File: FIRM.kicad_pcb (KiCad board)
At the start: 8 copper layers, 21.3 x 27 mm, 99 parts, among them J1 DM3CS-SF, J2 Conn_01x02_Pin, Q1 IRLML6402, U1 W25Q128JVS, U2 STM32F405RGTx, U3 ADXL371, U5 INA219AxDCN, U6 MIC5219-3.3YM5, U9 A-USBC-20F0-EA-GSR05, X1 32.768khz, Y1 12 MHz

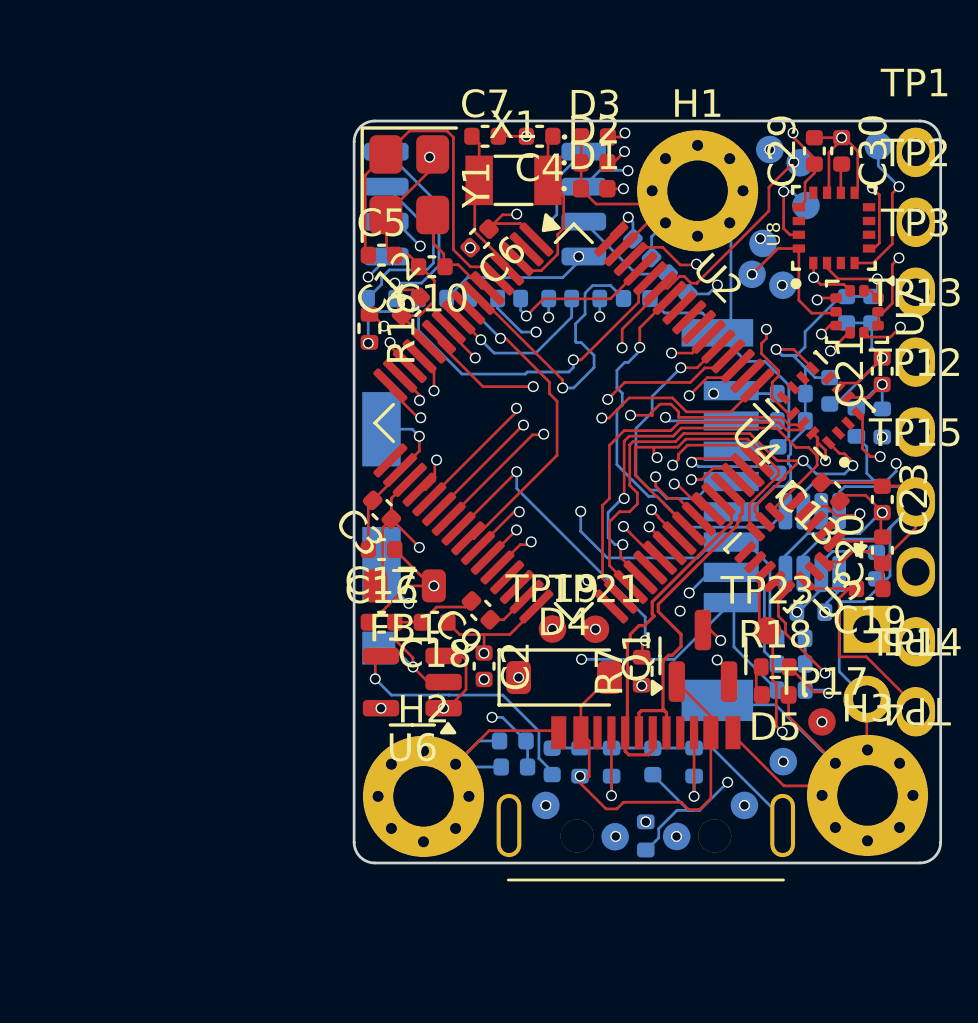
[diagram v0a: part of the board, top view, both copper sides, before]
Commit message: resistor arrays and smaller parts
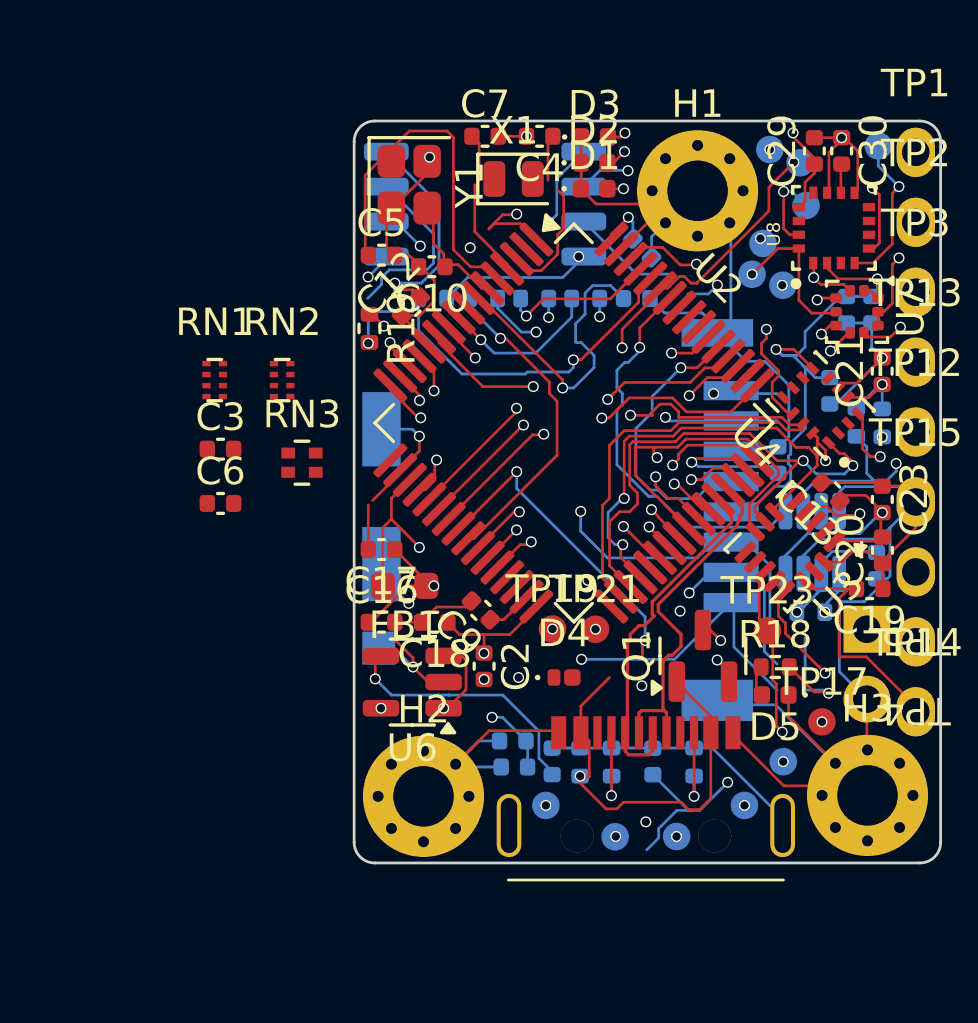
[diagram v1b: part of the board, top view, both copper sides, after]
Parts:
- removed R1, R5, R6, R7: 10k, Resistor_SMD:R_0402_1005Metric
- removed R10, R2, R4, R8, R9: 47k, Resistor_SMD:R_0402_1005Metric
- added RN1: 47k, connectors:R_Array_YC104, F.Cu at (148.3, 84.0)
- added RN2: 10k, connectors:R_Array_YC104, F.Cu at (150.7, 84.0)
- added RN3: 47k, connectors:R_Array_EXB-24V, F.Cu at (151.4, 87.0)
- D4: footprint Diode_SMD:D_SOD-123 -> connectors:D_schottky_NSR05F30NXT5G
- FB1: footprint Inductor_SMD:L_0805_2012Metric -> Inductor_SMD:L_0603_1608Metric
- X1: footprint Crystal:Crystal_SMD_3215-2Pin_3.2x1.5mm -> connectors:Crystal_ECS-.327-6-12RR-TR
- Y1: footprint Crystal:Crystal_SMD_Abracon_ABM8G-4Pin_3.2x2.5mm -> connectors:Crystal_ECS-120-10-36B2-CWY-TR
- moved C6 13.5 mm to (148.5, 88.5), turned to 0 degrees
- moved C3 6.27 mm to (148.5, 86.5), turned to 0 degrees

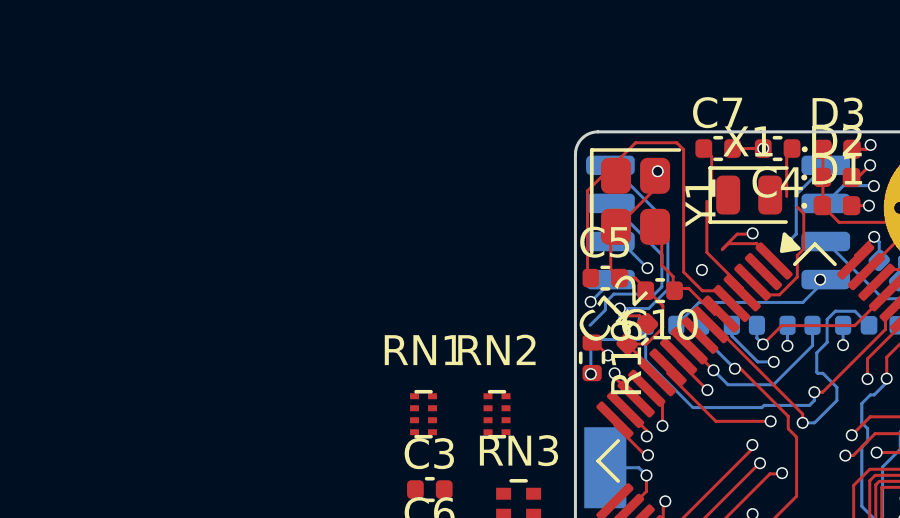
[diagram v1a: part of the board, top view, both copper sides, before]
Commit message: new flash chip
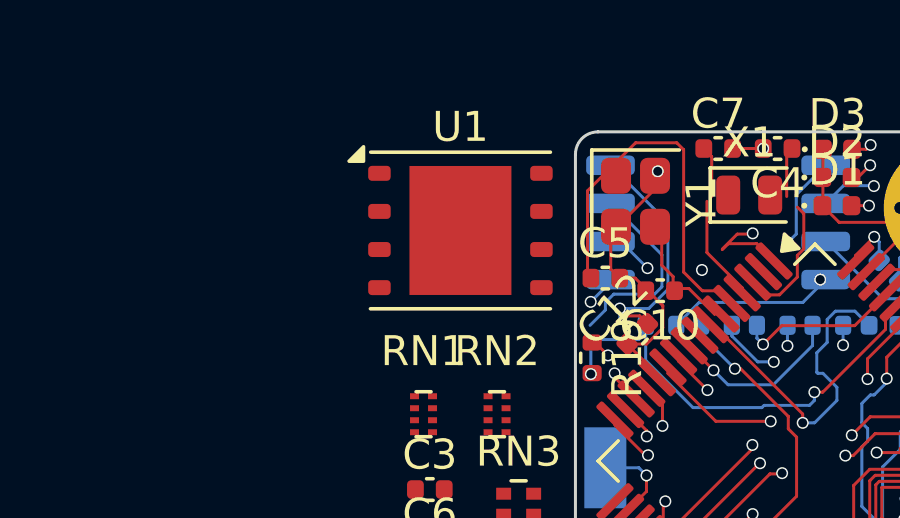
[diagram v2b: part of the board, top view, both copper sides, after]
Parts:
- added U1: W25Q128JVP, Package_SON:WSON-8-1EP_6x5mm_P1.27mm_EP3.4x4.3mm, F.Cu at (149.5, 77.9)

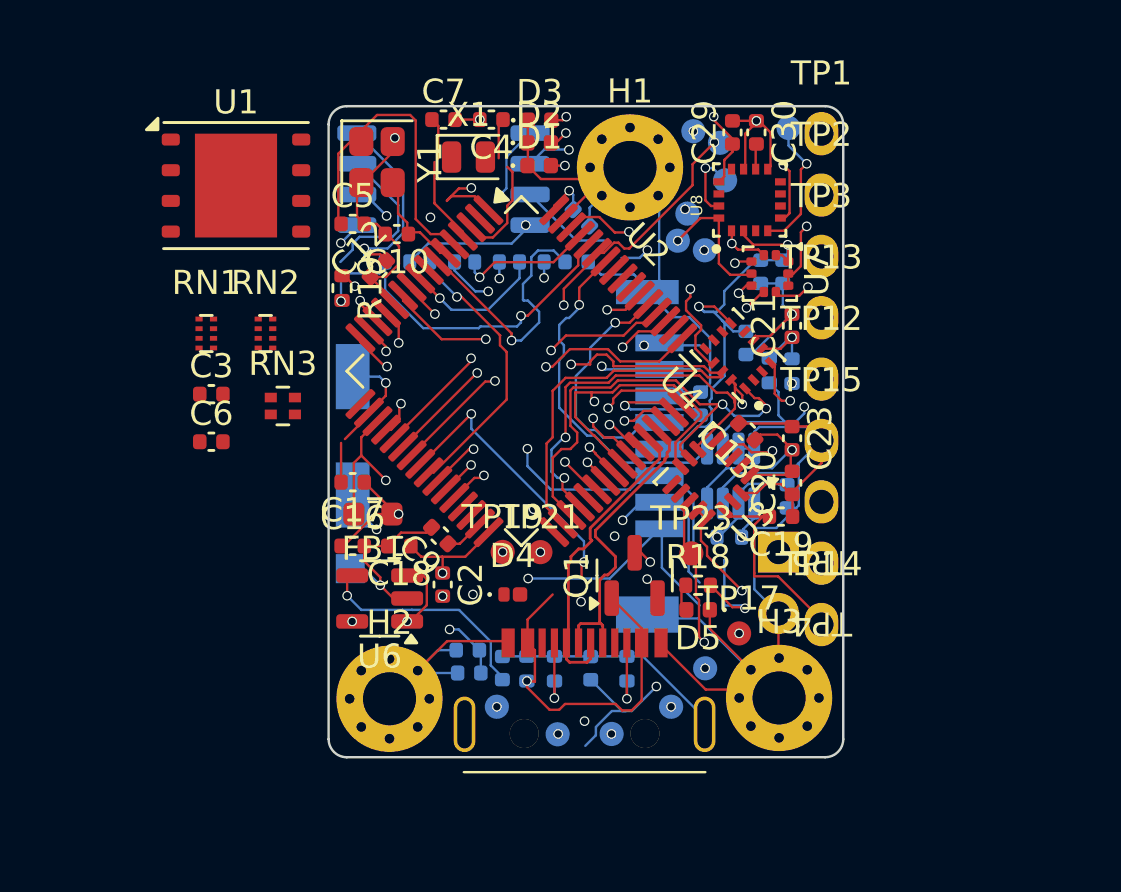
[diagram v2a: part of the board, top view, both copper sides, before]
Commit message: cleanup and improved decoupling capacitor locations
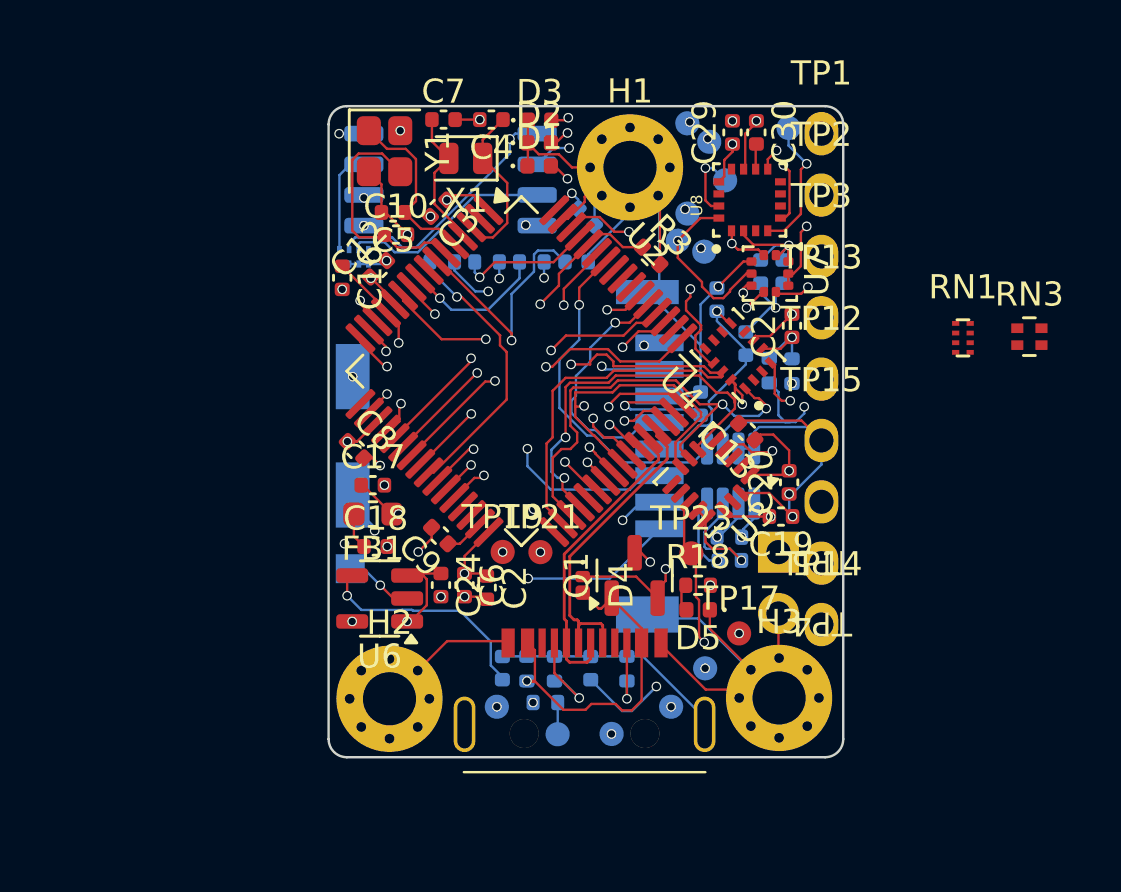
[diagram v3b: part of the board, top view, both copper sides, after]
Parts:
- removed the U1 at (149.5, 77.9)
- removed the U1 at (158.1, 77.6)
- added U1: W25Q128JVP, Package_SO:SOIC-8_5.3x5.3mm_P1.27mm, B.Cu at (158.4, 77.6)
- C23, R19, RN2: moved to B.Cu
- C24, C8, R3: moved to F.Cu
- moved RN1 31.3 mm to (179.6, 84.2)
- moved RN3 31.0 mm to (182.3, 84.1)
- moved R19 19.1 mm to (162.3, 99.3), turned to 180 degrees
- moved C11 17.8 mm to (170.6, 84.4), turned to -90 degrees
- moved C24 14.8 mm to (158.0, 94.4)
- moved C3 12.2 mm to (157.9, 78.8), turned to -135 degrees
- moved C6 12.0 mm to (159.0, 94.4), turned to -90 degrees
- moved C16 11.1 mm to (153.9, 81.7), turned to -90 degrees
- moved R3 10.5 mm to (166.7, 80.8), turned to -45 degrees
- moved C8 9.51 mm to (154.4, 88.8), turned to -45 degrees
- moved C23 5.68 mm to (169.9, 93.4), turned to 180 degrees
- moved RN2 4.85 mm to (154.4, 80.8), turned to -90 degrees
- moved D4 2.92 mm to (163.9, 94.4), turned to -90 degrees
- moved C22 2.16 mm to (169.4, 82.6), turned to 90 degrees
- moved C2 1.83 mm to (159.9, 94.5)
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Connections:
- RN1 pad 1: /SDIO_D0 -> /SDIO_D2
- RN1 pad 2: /SDIO_CMD -> /SDIO_D3
- RN1 pad 3: /SDIO_D3 -> /SDIO_CMD
- RN1 pad 4: /SDIO_D2 -> /SDIO_D0
- RN2 pad 2: Net-(RN2-R2.1) -> /FLASH_CS
- RN2 pad 3: /FLASH_CS -> Net-(RN2-R3.1)
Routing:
- net +3.3V: track 91.5 -> 55.8 mm
- net GND: track 142.1 -> 109.7 mm, vias 12 -> 26
- net Net-(R19-Pad1): track 23.6 -> 1.31 mm, vias 2 -> 0
- net /SD_DETECT: track 22.5 -> 9.67 mm, vias 3 -> 2
- net /BOOT0: track 14.5 -> 25.1 mm
- net Net-(RN2-R3.1): track 0.00 -> 8.81 mm
- net /I2C1_SDA: track 29.1 -> 35.4 mm
- net /HSE_OUT: track 3.54 -> 9.08 mm
- net /VSENS_IN: track 14.3 -> 9.05 mm, vias 3 -> 2
- net /SDIO_CMD: track 21.6 -> 16.4 mm
- net /HSE_IN: track 12.3 -> 7.44 mm
- net /SDIO_D3: track 19.6 -> 15.2 mm
- net /SDIO_D2: track 23.7 -> 19.8 mm
- net Net-(RN2-R2.1): track 3.85 -> 0.00 mm
- net Net-(RN2-R1.1): track 6.56 -> 3.71 mm
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
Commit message: added back resistors
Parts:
- removed RN1: 47k, connectors:R_Array_YC104
- removed RN3: 47k, connectors:R_Array_EXB-24V
- added R1: 47k, Resistor_SMD:R_0402_1005Metric, F.Cu at (177.2, 84.0)
- added R2: 47k, Resistor_SMD:R_0402_1005Metric, F.Cu at (177.2, 85.4)
- added R4: 47k, Resistor_SMD:R_0402_1005Metric, F.Cu at (177.2, 87.4)
- added R5: 47k, Resistor_SMD:R_0402_1005Metric, F.Cu at (177.2, 89.4)
- added R6: 47k, Resistor_SMD:R_0402_1005Metric, F.Cu at (162.0, 94.9)
- added R7: 47k, Resistor_SMD:R_0402_1005Metric, B.Cu at (159.0, 97.2)
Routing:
- net /SDIO_D1: track 7.58 -> 19.8 mm, vias 2 -> 3
- net /SD_DETECT: track 9.67 -> 21.6 mm, vias 2 -> 1
- net /SDIO_D0: track 8.51 -> 6.93 mm, vias 2 -> 1

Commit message: finished routing resistors
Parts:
- R1, R2, R4, R5: moved to B.Cu
- moved R1 14.5 mm to (169.2, 96.2)
- moved R2 12.7 mm to (169.2, 95.2)
- moved R4 10.5 mm to (169.2, 94.3)
- moved R5 9.24 mm to (169.2, 84.6)
- moved C11 3.13 mm to (168.7, 86.9)
- moved C14 1.42 mm to (169.2, 85.6), turned to 0 degrees
- moved TP17 0.07 mm to (170.3, 96.5)
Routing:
- net /SDIO_CMD: track 16.4 -> 21.9 mm
- net /SDIO_D3: track 15.2 -> 20.6 mm
- net +3.3V: track 55.8 -> 61.0 mm, vias 18 -> 20
- net /SDIO_D2: track 19.8 -> 24.6 mm
- net /SDIO_D0: track 6.93 -> 10.7 mm, vias 1 -> 2
- net /VCAP2: track 5.00 -> 5.78 mm
- net /SD_DETECT: track 21.6 -> 22.1 mm, vias 1 -> 2

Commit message: a lil bit of this a lil bit of that
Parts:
- R3: moved to B.Cu
- moved R3 19.0 mm to (159.3, 98.3), turned to 180 degrees
- moved TP7 0.57 mm to (167.3, 80.5)
- moved C26 0.22 mm to (160.7, 97.9)
- moved R16 0.12 mm to (161.7, 97.9)
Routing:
- net VBUS: track 14.1 -> 11.9 mm
- net /MOSI2: track 36.3 -> 37.7 mm
- net /FLASH_CS: track 26.0 -> 26.7 mm
- net GND: track 109.6 -> 110.1 mm

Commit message: changes
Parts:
- moved C12 5.49 mm to (153.9, 76.0), turned to -90 degrees
- moved Y1 0.25 mm to (155.9, 76.4)
- moved C7 0.23 mm to (158.3, 75.1)
- moved C4 0.12 mm to (160.2, 75.1)
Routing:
- net GND: track 110.1 -> 117.4 mm
- net /SCK2: track 51.2 -> 44.8 mm
- net /PA9: track 15.1 -> 16.4 mm
- net /HSE_OUT: track 9.08 -> 7.71 mm
- net VBUS: track 11.9 -> 13.0 mm

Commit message: silkscreen
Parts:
- removed R1: 47k, Resistor_SMD:R_0402_1005Metric
- added G***: LOGO, connectors:firm-logo, F.Cu at (168.2, 80.8)
- moved C12 5.49 mm to (155.4, 81.3), turned to 45 degrees
- moved Y1 0.25 mm to (155.7, 76.4)
- moved C7 0.23 mm to (158.1, 75.1)
- moved C4 0.12 mm to (160.1, 75.1)
- renumbered TP1 to A0, TP2 to A1, TP17 to BMP_CS, TP15 to GD, TP16 to IMU, TP18 to MAG, TP8 to SPI, TP13 to SWCLK, TP6 to a4
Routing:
- net GND: track 117.4 -> 110.1 mm
- net /SCK2: track 44.8 -> 51.2 mm
- net /PA9: track 16.4 -> 15.1 mm
- net /HSE_OUT: track 7.71 -> 9.08 mm
- net VBUS: track 13.0 -> 11.9 mm
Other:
- board text added: "+"
- board text added: "-"
- board text added: "I2C"
- board text removed: "FIRM v0.1"
